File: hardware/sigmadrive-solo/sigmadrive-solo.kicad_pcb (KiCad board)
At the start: 4 copper layers, 70.7 x 87.3 mm, 164 parts, among them J1 CONN_01X02, J10 Conn_01x03, J11 Conn_01x03, J12 Conn_01x05, J2 CONN_02X05, J4 Conn_01x05, J5 Conn_01x05, J6 629_105_150_921, J8 Conn_01x03, J9 Conn_01x03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

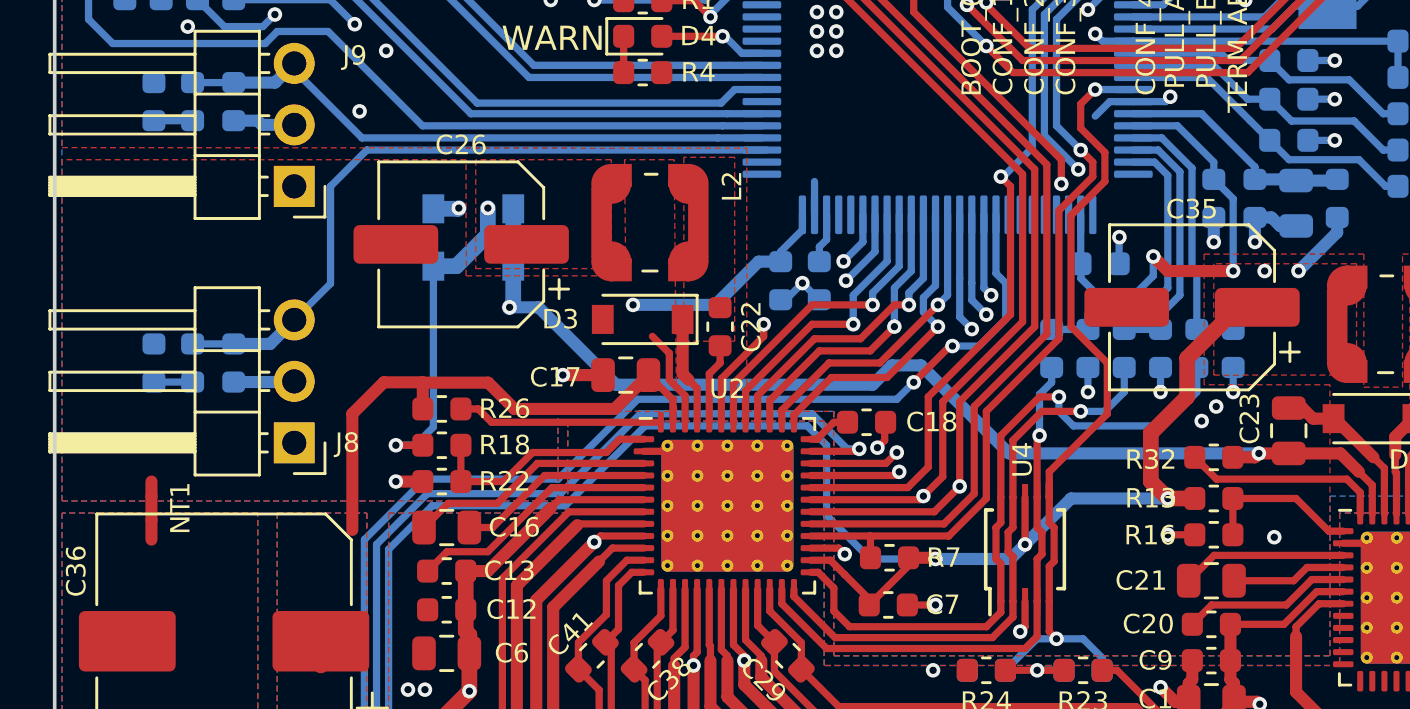
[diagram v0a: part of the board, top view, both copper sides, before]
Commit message: Added second net-tie between GND and PGND.
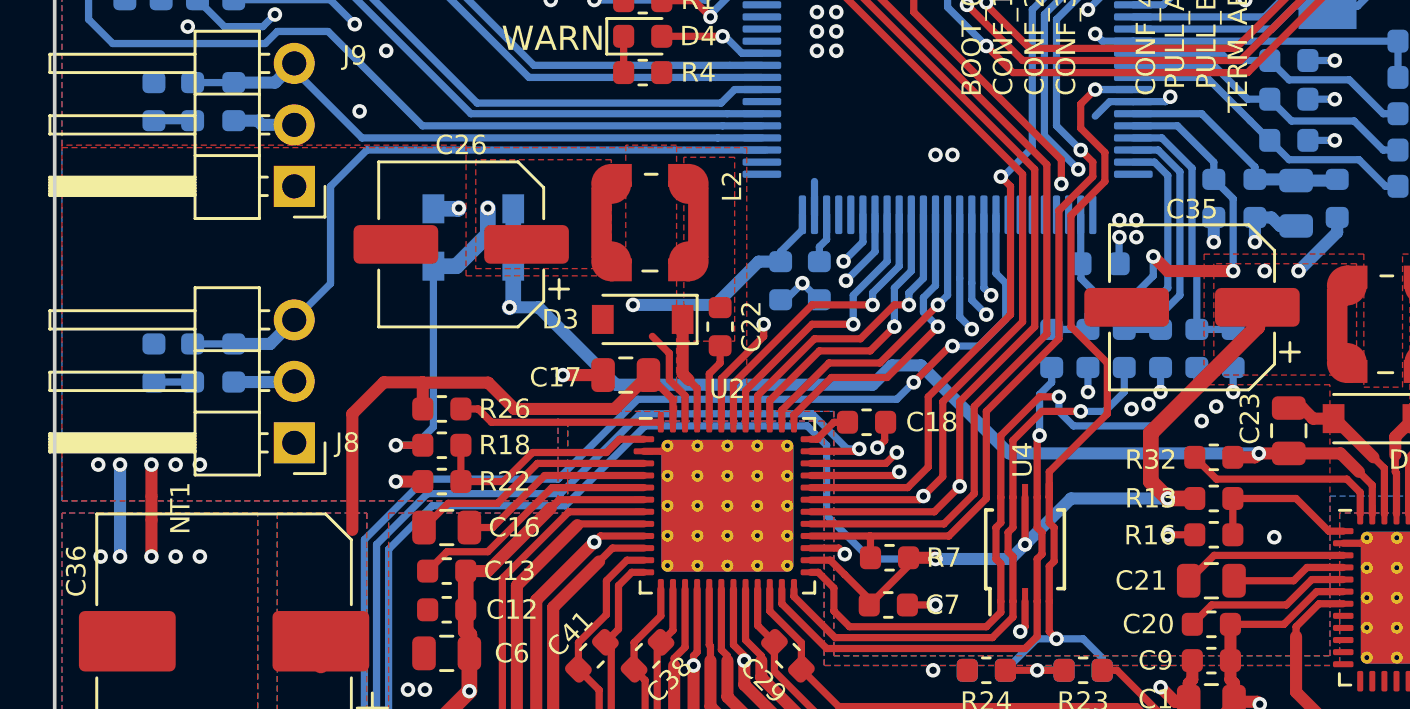
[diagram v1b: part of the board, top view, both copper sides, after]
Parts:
- added NT3: Net-Tie_2, NetTie:NetTie-2_SMD_Pad0.5mm, B.Cu at (79.2, 74.7)
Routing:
- net PGND: track 6.11 -> 8.31 mm, vias 51 -> 56
- net GND: track 137.1 -> 139.1 mm, vias 50 -> 62
- net +3V3: track 401.2 -> 400.2 mm
- net /MOSFETs/PHASE_B: track 75.2 -> 74.7 mm
- net /MOSFETs/PHASE_C: track 90.7 -> 90.2 mm

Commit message: Routed version 3.4
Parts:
- removed NT3: Net-Tie_2, NetTie:NetTie-2_SMD_Pad0.5mm
- added C46: 4.7uF 50V, Capacitor_SMD:C_0805_2012Metric, B.Cu at (127.5, 46.2)
- added C47: 10uF 35V, Capacitor_SMD:C_1206_3216Metric, F.Cu at (95.5, 62.4)
- added C48: 10uF 35V, Capacitor_SMD:C_1206_3216Metric, F.Cu at (125.6, 68.7)
- added C49: 4.7uF 50V, Capacitor_SMD:C_0805_2012Metric, B.Cu at (129.5, 46.2)
- added C50: 1uF 100V, Capacitor_SMD:C_0805_2012Metric, F.Cu at (140.2, 72.4)
- added C56: 4.7uF 50V, Capacitor_SMD:C_0805_2012Metric, F.Cu at (141.1, 65.4)
- added D8: BAT30KFILM, Diode_SMD:D_SOD-523, F.Cu at (136.3, 65.4)
- added FB2: 0.6OHM/0.2A/2.2 kOhm, Resistor_SMD:R_0603_1608Metric, B.Cu at (131.3, 46.2)
- added FB3: 0.6OHM/0.2A/2.2 kOhm, Resistor_SMD:R_0603_1608Metric, F.Cu at (125.4, 72.4)
- added FB4: 0.6OHM/0.2A/2.2 kOhm, Resistor_SMD:R_0603_1608Metric, F.Cu at (95.3, 67.4)
- added JP1: Jumper_2_Open, Jumper:SolderJumper-2_P1.3mm_Open_TrianglePad1.0x1.5mm, B.Cu at (78.7, 74.9)
- added JP2: Jumper_2_Open, Jumper:SolderJumper-2_P1.3mm_Open_TrianglePad1.0x1.5mm, F.Cu at (144.3, 84.1)
- added R36: N/A, Resistor_SMD:R_0603_1608Metric, F.Cu at (139.2, 65.6)
- added R39: 0, Resistor_SMD:R_0603_1608Metric, F.Cu at (133.0, 64.8)
- added R41: N/A, Resistor_SMD:R_0603_1608Metric, F.Cu at (120.7, 73.1)
- added TP10: PAD, TestPoint:TestPoint_Pad_D1.0mm, F.Cu at (142.7, 61.3)
- added U7: TPS70933, Package_TO_SOT_SMD:SOT-23-5, F.Cu at (140.2, 69.3)
- C26, C35: value 100uF -> 10uF 35V; footprint Capacitor_SMD:CP_Elec_6.3x7.7 -> Capacitor_SMD:C_1206_3216Metric
- C27, C32: value 27pF/50V/1% -> 7pF/50V/1%
- FB1: value 0.6OHM/0.2A/2.2 kOhm @ 100MHz -> 0.6OHM/0.2A/2.2 kOhm
- Y1: value ABM3-8.000MHZ-D2Y-T -> NX3225SA-12.000M-STD-CSR-1; footprint Crystal:Crystal_SMD_Abracon_ABM3-2Pin_5.0x3.2mm -> Crystal:Crystal_SMD_3225-4Pin_3.2x2.5mm
- moved F2 8.97 mm to (92.0, 39.7)
- moved F4 8.97 mm to (92.0, 39.7)
- moved R21 7.99 mm to (134.1, 60.6), turned to 0 degrees
- moved D6 7.16 mm to (134.1, 62.1), turned to 180 degrees
- moved USR1 6.18 mm to (96.0, 47.9)
- moved C4 6.11 mm to (97.5, 45.4)
- moved R9 6.11 mm to (94.5, 45.4)
- moved D1 5.22 mm to (95.9, 50.4), turned to 180 degrees
- moved D4 5.22 mm to (95.9, 53.4)
- moved R1 5.22 mm to (95.9, 51.9)
- moved R4 5.22 mm to (95.9, 54.9)
- moved C35 4.96 mm to (127.9, 68.7), turned to 270 degrees
- moved C26 4.81 mm to (97.9, 62.4), turned to 270 degrees
- moved R10 4.38 mm to (99.6, 47.7), turned to 270 degrees
- moved D7 3.96 mm to (91.1, 61.8), turned to 0 degrees
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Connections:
- C14 pad 2: +3V3 -> +3.3VP
- C17 pad 1: VIN -> Net-(C17-Pad1)
- C19 pad 2: +3V3 -> +3.3VP
- C23 pad 1: +5V -> Net-(C23-Pad1)
- C24 pad 2: +3V3 -> +3.3VP
- C28 pad 1: +3V3 -> +3.3VP
- C35 pad 1: +3V3 -> Net-(C35-Pad1)
- C53 pad 2: +3V3 -> +3.3VP
- C54 pad 2: +3V3 -> +3.3VP
- C55 pad 2: +3V3 -> +3.3VP
- L1 pad 2: +3V3 -> Net-(C35-Pad1)
- R13 pad 2: +3V3 -> Net-(C35-Pad1)
- R26 pad 1: VIN -> Net-(C17-Pad1)
- R32 pad 1: +5V -> Net-(C23-Pad1)
- U1 pad 47: +5V -> Net-(C23-Pad1)
- U2 pad 47: VIN -> Net-(C17-Pad1)
- U5 pad 100: +3V3 -> +3.3VP
- U5 pad 11: +3V3 -> +3.3VP
- U5 pad 21: +3V3 -> +3.3VP
- U5 pad 27: +3V3 -> +3.3VP
- U5 pad 50: +3V3 -> +3.3VP
- U5 pad 6: +3V3 -> +3.3VP
- U5 pad 75: +3V3 -> +3.3VP
- Y1 pad 1: Net-(C32-Pad1) -> Net-(C27-Pad1)
- Y1 pad 2: Net-(C27-Pad1) -> GND
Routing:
- net +3.3VP: track 0.00 -> 134.9 mm, vias 0 -> 6
- net +3V3: track 400.2 -> 360.8 mm, vias 18 -> 19
- net GND: track 139.1 -> 170.1 mm, vias 62 -> 73
- net Net-(C35-Pad1): track 0.00 -> 20.9 mm, vias 0 -> 2
- net Net-(C17-Pad1): track 0.00 -> 13.3 mm
- net VIN: track 137.2 -> 127.8 mm, vias 49 -> 50
- net +5V: track 199.1 -> 208.0 mm, vias 3 -> 4
- net Net-(C23-Pad1): track 0.00 -> 8.31 mm
- net /MCU/LED_WARN: track 4.43 -> 10.1 mm
- net Net-(D8-Pad2): track 0.00 -> 5.50 mm
- net /MCU/LED_STATUS: track 4.89 -> 10.2 mm
- net /MCU/PA8: track 22.6 -> 17.7 mm
- net Net-(C26-Pad1): track 13.5 -> 17.3 mm, vias 2 -> 3
- net Net-(C56-Pad1): track 0.00 -> 3.75 mm
- net /MCU/ENCODER_DI: track 38.1 -> 34.7 mm
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- added copper zone on F.Cu, net Net-(C35-Pad1)
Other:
- board text added: "SIGMADRIVE-SOLO Ver 3.4"
- board text removed: "SIGMADRIVE-SOLO Ver 3.3"

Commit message: Routed version 3.4
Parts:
- moved F2 3.90 mm to (91.9, 43.6)
- moved F4 3.90 mm to (91.9, 43.6)
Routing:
- net +3.3VP: track 134.9 -> 134.4 mm
- net GND: vias 73 -> 74
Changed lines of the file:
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@@
     (thickness 1.6)
     (drawings 27)
-    (tracks 1815)
+    (tracks 1818)
     (zones 0)
     (modules 181)
@@
     (0 F.Cu mixed)
     (1 In1.Cu mixed)
-    (2 In2.Cu mixed hide)
+    (2 In2.Cu mixed)
     (31 B.Cu mixed)
     (32 B.Adhes user hide)
@@
   )
   (module Fiducials:Fiducial_0.5mm_Dia_1mm_Outer (layer F.Cu)
-    (at 92 39.7)
+    (at 91.9 43.6)
     (descr "Circular Fiducial, 0.5mm bare copper top; 1mm keepout (Level C)")
     (tags marker)
@@
   )
   (module Fiducials:Fiducial_0.5mm_Dia_1mm_Outer (layer B.Cu)
-    (at 92 39.7)
+    (at 91.9 43.6)
     (descr "Circular Fiducial, 0.5mm bare copper top; 1mm keepout (Level C)")
     (tags marker)
     (attr virtual)
-    (fp_text reference F4 (at 0 1.36745) (layer B.SilkS)
+    (fp_text reference F4 (at 0 -1.2) (layer B.SilkS)
       (effects (font (size 0.8 0.8) (thickness 0.15)) (justify mirror))
     )
@@
   (via (at 129.4 59.5) (size 0.6) (drill 0.3) (layers F.Cu B.Cu) (net 1))
   (segment (start 129.4 59.5) (end 128.2875 59.5) (width 0.3) (layer B.Cu) (net 1))
-  (segment (start 126.2 59.3) (end 112.4 59.3) (width 0.3) (layer In1.Cu) (net 1))
-  (segment (start 98.8 72.9) (end 98.8 76.1) (width 0.3) (layer In1.Cu) (net 1))
+  (segment (start 98.8 73.4) (end 98.8 76.1) (width 0.3) (layer In1.Cu) (net 1))
+  (segment (start 112.9 59.3) (end 98.8 73.4) (width 0.3) (layer In1.Cu) (net 1))
+  (segment (start 126.2 59.3) (end 112.9 59.3) (width 0.3) (layer In1.Cu) (net 1))
   (segment (start 129.4 59.5) (end 126.4 59.5) (width 0.3) (layer In1.Cu) (net 1))
-  (segment (start 112.4 59.3) (end 98.8 72.9) (width 0.3) (layer In1.Cu) (net 1))
   (segment (start 126.4 59.5) (end 126.2 59.3) (width 0.3) (layer In1.Cu) (net 1))
   (segment (start 102.9 81.2) (end 102.9 81.2) (width 0.5) (layer F.Cu) (net 2))
@@
   (via (at 129.4 57.8) (size 0.6) (drill 0.3) (layers F.Cu B.Cu) (net 2))
   (segment (start 129.4 57.8) (end 128.2875 57.8) (width 0.3) (layer B.Cu) (net 2))
+  (segment (start 98 73.5) (end 98 76.3) (width 0.3) (layer In1.Cu) (net 2))
   (segment (start 98 76.3) (end 102.9 81.2) (width 0.3) (layer In1.Cu) (net 2))
-  (segment (start 112.2 58.8) (end 98 73) (width 0.3) (layer In1.Cu) (net 2))
-  (segment (start 98 73) (end 98 76.3) (width 0.3) (layer In1.Cu) (net 2))
-  (segment (start 126.1 58.8) (end 112.2 58.8) (width 0.3) (layer In1.Cu) (net 2))
+  (segment (start 112.7 58.8) (end 98 73.5) (width 0.3) (layer In1.Cu) (net 2))
+  (segment (start 126.1 58.8) (end 112.7 58.8) (width 0.3) (layer In1.Cu) (net 2))
   (segment (start 129.4 57.8) (end 127.1 57.8) (width 0.3) (layer In1.Cu) (net 2))
   (segment (start 127.1 57.8) (end 126.1 58.8) (width 0.3) (layer In1.Cu) (net 2))
@@
   (segment (start 102.6 81.8) (end 104.2 81.8) (width 0.3) (layer In1.Cu) (net 3))
   (segment (start 128 56.2) (end 125.9 58.3) (width 0.3) (layer In1.Cu) (net 3))
-  (segment (start 125.9 58.3) (end 112 58.3) (width 0.3) (layer In1.Cu) (net 3))
   (segment (start 129.4 56.2) (end 128 56.2) (width 0.3) (layer In1.Cu) (net 3))
-  (segment (start 112 58.3) (end 97.5 72.8) (width 0.3) (layer In1.Cu) (net 3))
-  (segment (start 97.5 72.8) (end 97.5 76.7) (width 0.3) (layer In1.Cu) (net 3))
+  (segment (start 125.9 58.3) (end 112.5 58.3) (width 0.3) (layer In1.Cu) (net 3))
   (segment (start 97.5 76.7) (end 102.6 81.8) (width 0.3) (layer In1.Cu) (net 3))
+  (segment (start 112.5 58.3) (end 97.5 73.3) (width 0.3) (layer In1.Cu) (net 3))
+  (segment (start 97.5 73.3) (end 97.5 76.7) (width 0.3) (layer In1.Cu) (net 3))
   (segment (start 86.23 36.72) (end 85.675 36.72) (width 0.3) (layer F.Cu) (net 4))
   (segment (start 86.6 36.35) (end 86.23 36.72) (width 0.3) (layer F.Cu) (net 4))
@@
   (via (at 80.5 72.9) (size 0.6) (drill 0.3) (layers F.Cu B.Cu) (net 4))
   (via (at 81.5 72.9) (size 0.6) (drill 0.3) (layers F.Cu B.Cu) (net 4))
-  (via (at 112.9 60.1) (size 0.6) (drill 0.3) (layers F.Cu B.Cu) (net 4))
+  (via (at 114.3 60.1) (size 0.6) (drill 0.3) (layers F.Cu B.Cu) (net 4))
   (via (at 113.6 60.1) (size 0.6) (drill 0.3) (layers F.Cu B.Cu) (net 4))
   (via (at 121.7 70.4) (size 0.6) (drill 0.3) (layers F.Cu B.Cu) (net 4))
@@
   (segment (start 128.7625 71.9625) (end 129.1 72.3) (width 1) (layer F.Cu) (net 4))
   (segment (start 125.6 70.1) (end 127.9 70.1) (width 1) (layer F.Cu) (net 4))
+  (via (at 136.3 74.4) (size 0.6) (drill 0.3) (layers F.Cu B.Cu) (net 4))
   (segment (start 97 53.4) (end 96.6875 53.4) (width 0.3) (layer F.Cu) (net 5))
   (segment (start 98.5 54.9) (end 97 53.4) (width 0.3) (layer F.Cu) (net 5))
@@
   (segment (start 132 54.5) (end 132 59.6) (width 1) (layer In1.Cu) (net 188))
   (segment (start 132 59.6) (end 129.7 61.9) (width 1) (layer In1.Cu) (net 188))
-  (segment (start 119.6 64.2) (end 119.6 65.6) (width 1) (layer In2.Cu) (net 188))
-  (segment (start 118 62.6) (end 119.6 64.2) (width 1) (layer In2.Cu) (net 188))
-  (via (at 105.6 62.6) (size 0.6) (drill 0.3) (layers F.Cu B.Cu) (net 188))
-  (segment (start 105.6 62.6) (end 118 62.6) (width 1) (layer In2.Cu) (net 188))
   (segment (start 105.6 47.4) (end 106 47) (width 1) (layer In1.Cu) (net 188))
-  (segment (start 105.6 62.6) (end 105.6 47.4) (width 1) (layer In1.Cu) (net 188))
   (segment (start 105.6 47.4) (end 104.3 47.4) (width 0.5) (layer In1.Cu) (net 188))
   (segment (start 103.9 47) (end 103.1 47) (width 0.5) (layer In1.Cu) (net 188))
   (segment (start 104.3 47.4) (end 103.9 47) (width 0.5) (layer In1.Cu) (net 188))
-  (segment (start 105.6 63.9125) (end 106.2 64.5125) (width 0.5) (layer B.Cu) (net 188))
-  (segment (start 105.6 62.6) (end 105.6 63.9125) (width 0.5) (layer B.Cu) (net 188))
   (segment (start 106.2 64.5125) (end 106.7875 64.5125) (width 0.3) (layer B.Cu) (net 188))
   (segment (start 107.4 63.9) (end 107.4 62.575) (width 0.3) (layer B.Cu) (net 188))
   (segment (start 106.7875 64.5125) (end 107.4 63.9) (width 0.3) (layer B.Cu) (net 188))
+  (segment (start 105.6 61.5) (end 105.6 47.4) (width 1) (layer In1.Cu) (net 188))
+  (segment (start 106.4 62.3) (end 105.6 61.5) (width 1) (layer In1.Cu) (net 188))
+  (segment (start 106.4 62.3) (end 106.2 62.5) (width 0.5) (layer B.Cu) (net 188))
+  (via (at 106.4 62.3) (size 0.6) (drill 0.3) (layers F.Cu B.Cu) (net 188))
+  (segment (start 119.6 64.2) (end 119.6 65.6) (width 1) (layer In2.Cu) (net 188))
+  (segment (start 106.2 62.5) (end 106.2 64.5125) (width 0.5) (layer B.Cu) (net 188))
+  (segment (start 106.4 62.3) (end 106.7 62.6) (width 1) (layer In2.Cu) (net 188))
+  (segment (start 106.7 62.6) (end 118 62.6) (width 1) (layer In2.Cu) (net 188))
+  (segment (start 118 62.6) (end 119.6 64.2) (width 1) (layer In2.Cu) (net 188))
   (zone (net 36) (net_name VIN) (layer F.Cu) (hatch edge 0.508)
     (connect_pads yes (clearance 0.25))

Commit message: Review from ZEK.
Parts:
- removed C28: 1uF 100V, Capacitor_SMD:C_0805_2012Metric
- removed C53: 100nF 50V, Capacitor_SMD:C_0603_1608Metric
- removed C56: 4.7uF 50V, Capacitor_SMD:C_0805_2012Metric
- removed D8: BAT30KFILM, Diode_SMD:D_SOD-523
- removed FB2, FB3, FB4: 0.6OHM/0.2A/2.2 kOhm, Resistor_SMD:R_0603_1608Metric
- removed JP1, JP2: Jumper_2_Open, Jumper:SolderJumper-2_P1.3mm_Open_TrianglePad1.0x1.5mm
- removed R36: N/A, Resistor_SMD:R_0603_1608Metric
- removed R39: 0, Resistor_SMD:R_0603_1608Metric
- removed TP10: PAD, TestPoint:TestPoint_Pad_D1.0mm
- added NT3: Net-Tie_2, NetTie:NetTie-2_SMD_Pad0.5mm, B.Cu at (77.9, 74.7)
- C47: value 10uF 35V -> 1000pF/50V; footprint Capacitor_SMD:C_1206_3216Metric -> Capacitor_SMD:C_0603_1608Metric; moved to B.Cu
- C48: value 10uF 35V -> 100nF 50V; footprint Capacitor_SMD:C_1206_3216Metric -> Capacitor_SMD:C_0603_1608Metric; moved to B.Cu
- C49: value 4.7uF 50V -> 7pF/50V/5%; footprint Capacitor_SMD:C_0805_2012Metric -> Capacitor_SMD:C_0603_1608Metric
- C50: value 1uF 100V -> 7pF/50V/5%; footprint Capacitor_SMD:C_0805_2012Metric -> Capacitor_SMD:C_0603_1608Metric; moved to B.Cu
- U7: value TPS70933 -> TPD4S009; footprint Package_TO_SOT_SMD:SOT-23-5 -> Package_SO:TSSOP-10_3x3mm_P0.5mm; moved to B.Cu
- moved U7 53.9 mm to (91.5, 46.2), turned to 270 degrees
- moved C50 53.8 mm to (94.1, 44.7), turned to 90 degrees
- moved C49 40.6 mm to (88.9, 44.7), turned to 90 degrees
- moved C48 37.9 mm to (94.1, 47.7), turned to 90 degrees
- moved R35 24.0 mm to (116.2, 68.1), turned to 270 degrees
- moved C47 21.3 mm to (116.7, 64.6), turned to 180 degrees
- moved F2 20.3 mm to (93.3, 23.3)
- moved F4 20.3 mm to (93.3, 23.3)
- moved R21 6.80 mm to (140.3, 63.4), turned to 180 degrees
- moved D6 6.20 mm to (140.3, 61.9), turned to 0 degrees
- moved C46 4.83 mm to (122.8, 45.1), turned to 0 degrees
- moved R10 2.63 mm to (100.7, 45.3), turned to 180 degrees
- moved NT1 2.60 mm to (77.9, 74.7)
- moved RV1 2.00 mm to (115.7, 92.0)
- moved C4 0.14 mm to (97.6, 45.3), turned to 180 degrees
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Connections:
- C14 pad 2: +3.3VP -> +3V3
- C17 pad 1: Net-(C17-Pad1) -> VIN
- C19 pad 2: +3.3VP -> +3V3
- C23 pad 1: Net-(C23-Pad1) -> +5V
- C24 pad 2: +3.3VP -> +3V3
- C35 pad 1: Net-(C35-Pad1) -> +3V3
- C4 pad 1: Net-(C4-Pad1) -> GND
- C46 pad 1: +3.3VP -> +3V3
- C47 pad 1: Net-(C26-Pad1) -> GND
- C47 pad 2: GND -> /MCU/PB0
- C48 pad 1: Net-(C35-Pad1) -> +3V3
- C49 pad 1: +3.3VP -> GND
- C49 pad 2: GND -> Net-(C49-Pad2)
- C50 pad 1: +5V -> GND
- C50 pad 2: GND -> Net-(C50-Pad2)
- C54 pad 2: +3.3VP -> +3V3
- C55 pad 2: +3.3VP -> +3V3
- J6 pad 2: Net-(J6-Pad2) -> Net-(C49-Pad2)
- J6 pad 3: Net-(J6-Pad3) -> Net-(C50-Pad2)
- L1 pad 2: Net-(C35-Pad1) -> +3V3
- R13 pad 2: Net-(C35-Pad1) -> +3V3
- R26 pad 1: Net-(C17-Pad1) -> VIN
- R32 pad 1: Net-(C23-Pad1) -> +5V
- R35 pad 1: GND -> /MCU/PB0
- R35 pad 2: /MCU/PB0 -> +3V3
- R47 pad 1: Net-(J6-Pad2) -> Net-(C49-Pad2)
- R50 pad 1: Net-(J6-Pad3) -> Net-(C50-Pad2)
- R9 pad 1: GND -> Net-(R9-Pad1)
- R9 pad 2: Net-(C4-Pad1) -> /MCU/PA8
- RV1 pad 1: +3V3 -> /MCU/PB0
- RV1 pad 2: /MCU/PB0 -> GND
- U1 pad 47: Net-(C23-Pad1) -> +5V
- U2 pad 47: Net-(C17-Pad1) -> VIN
- U5 pad 100: +3.3VP -> +3V3
- U5 pad 11: +3.3VP -> +3V3
- U5 pad 21: +3.3VP -> Net-(C30-Pad1)
- U5 pad 27: +3.3VP -> +3V3
- U5 pad 50: +3.3VP -> +3V3
- U5 pad 6: +3.3VP -> +3V3
- U5 pad 75: +3.3VP -> +3V3
- U7 pad 1: +5V -> Net-(C49-Pad2)
- U7 pad 2: GND -> Net-(C50-Pad2)
- U7 pad 3: Net-(U7-Pad3) -> GND
- USR1 pad 2: /MCU/PA8 -> Net-(R9-Pad1)
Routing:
- net +3.3VP: track 134.4 -> 0.00 mm, vias 6 -> 0
- net PGND: track 5.70 -> 76.1 mm, vias 49 -> 67
- net +3V3: track 360.8 -> 400.3 mm, vias 19 -> 22
- net Net-(C50-Pad2): track 0.00 -> 30.5 mm, vias 0 -> 1
- net Net-(C49-Pad2): track 0.00 -> 29.0 mm, vias 0 -> 1
- net Net-(J6-Pad2): track 28.0 -> 0.00 mm, vias 1 -> 0
- net Net-(J6-Pad3): track 26.6 -> 0.00 mm, vias 1 -> 0
- net Net-(C35-Pad1): track 20.9 -> 0.00 mm, vias 2 -> 0
- net Net-(C17-Pad1): track 13.3 -> 0.00 mm
- net +5V: track 208.0 -> 199.5 mm, vias 4 -> 3
- net Net-(C23-Pad1): track 8.31 -> 0.00 mm
- net VIN: track 127.8 -> 135.3 mm
- net GND: track 170.1 -> 177.4 mm, vias 74 -> 75
- net Net-(R9-Pad1): track 0.00 -> 5.57 mm
- net Net-(D8-Pad2): track 5.50 -> 0.00 mm
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- removed copper zone on F.Cu, net Net-(C35-Pad1)
